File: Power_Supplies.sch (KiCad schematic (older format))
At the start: 25 parts, among them U4 BD50FC0WEFJ-E2, U5 LDL212D33R, U6 LDL212D33R

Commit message: Stuff
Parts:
- gave numbers to parts that had none: 11

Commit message: Finished schemo and placement of power supply board, then resolved interconnects with the main board.
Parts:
- removed C21: 100nF_0603_Ceramic_Capacitor,_10%,_X7R,_25V, Capacitor_SMD:C_0603_1608Metric, symbol OpenVent:100nF_0603_Ceramic_Capacitor,_10%,_X7R,_25V
- removed R11: 10k_0603_Chip_Resistor,_1%,_0.1W, Resistor_SMD:R_0603_1608Metric, symbol OpenVent:10k_0603_Chip_Resistor,_1%,_0.1W
- removed R16, R17: 1K_0603_Chip_Resistor,_1%,_0.1W, Resistor_SMD:R_0603_1608Metric, symbol OpenVent:1K_0603_Chip_Resistor,_1%,_0.1W
- removed R8: 634R_0603_Chip_Resistor,_1%,_0.1W, Resistor_SMD:R_0603_1608Metric, symbol OpenVent:634R_0603_Chip_Resistor,_1%,_0.1W
- removed R9: 20k_0603_Chip_Resistor,_1%,_0.1W, Resistor_SMD:R_0603_1608Metric, symbol OpenVent:20k_0603_Chip_Resistor,_1%,_0.1W
- added R8: R_0603_200_0.1W_1%, Resistor_SMD:R_0603_1608Metric, symbol OpenVent:R_0603_200_0.1W_1%
- added R9: R_0603_24k9_0.1W_1%, symbol OpenVent:R_0603_24k9_0.1W_1%
- U7: footprint Package_SO:VSSOP-8_3.0x3.0mm_P0.65mm -> F_ICs:Texas_S-PDSO-G8
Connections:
- net labels added: FAN_DRIVE, MICROSWITCH_1, MICROSWITCH_2, MICROSWITCH_3
- net labels removed: VIN_12V, nLINE_PWR_FAULT
- wire segments 110 -> 105
- no-connect marks 1 -> 0
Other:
- moved on the sheet: D2, U7B

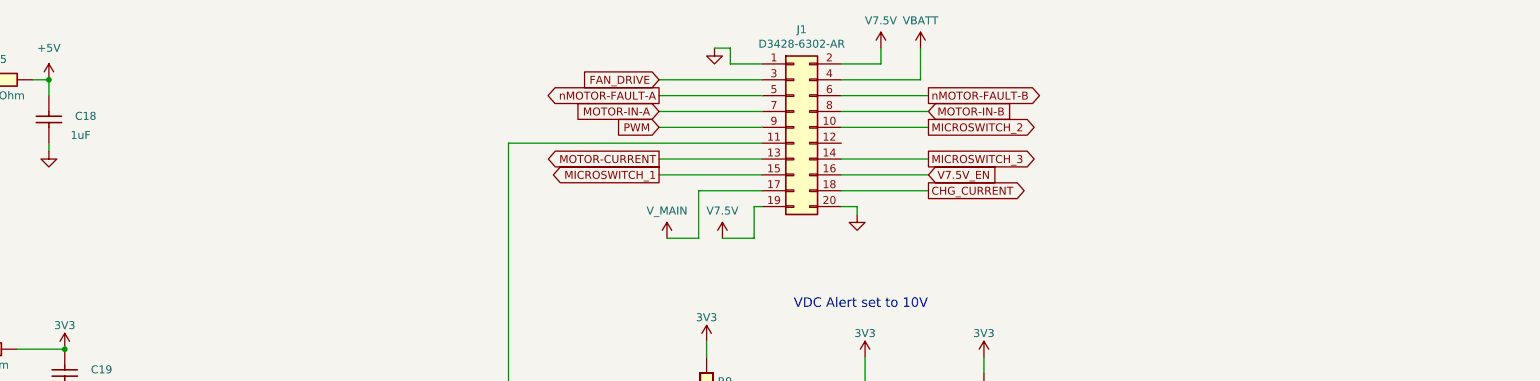
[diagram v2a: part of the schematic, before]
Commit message: Went through the whole circuit and made a note of what needs changing
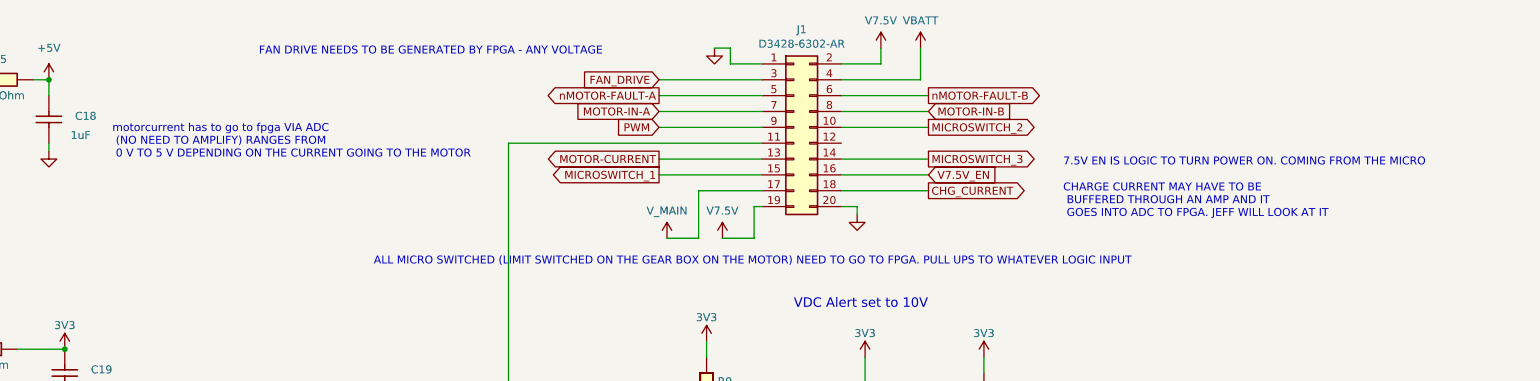
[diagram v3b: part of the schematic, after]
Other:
- note added: "7.5V EN IS LOGIC TO TURN POWER ON. COMING FROM THE MICRO"
- note added: "ALL MICRO SWITCHED (LIMIT SWITCHED ON THE GEAR BOX ON THE MOTOR) NEED TO GO TO FPGA. PULL UPS TO WHATEVER LOGIC INPUT"
- note added: "CHARGE CURRENT MAY HAVE TO BE\n BUFFERED THROUGH AN AMP AND IT\n GOES INTO ADC TO FPGA. JEFF WILL LOOK AT IT"
- note added: "FAN DRIVE NEEDS TO BE GENERATED BY FPGA - ANY VOLTAGE\n"
- note added: "motorcurrent has to go to fpga VIA ADC\n (NO NEED TO AMPLIFY) RANGES FROM\n 0 V TO 5 V DEPENDING ON THE CURRENT GOING TO THE MOTOR"
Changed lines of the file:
@@
 Wire Wire Line
 	9750 1700 9200 1700
+Text Notes 5525 1050 0    50   ~ 0
+FAN DRIVE NEEDS TO BE GENERATED BY FPGA - ANY VOLTAGE\n
+Text Notes 6250 2375 0    50   ~ 0
+ALL MICRO SWITCHED (LIMIT SWITCHED ON THE GEAR BOX ON THE MOTOR) NEED TO GO TO FPGA. PULL UPS TO WHATEVER LOGIC INPUT
+Text Notes 4600 1700 0    50   ~ 0
+motorcurrent has to go to fpga VIA ADC\n (NO NEED TO AMPLIFY) RANGES FROM\n 0 V TO 5 V DEPENDING ON THE CURRENT GOING TO THE MOTOR
+Text Notes 10600 2075 0    50   ~ 0
+CHARGE CURRENT MAY HAVE TO BE\n BUFFERED THROUGH AN AMP AND IT\n GOES INTO ADC TO FPGA. JEFF WILL LOOK AT IT
+Text Notes 10600 1750 0    50   ~ 0
+7.5V EN IS LOGIC TO TURN POWER ON. COMING FROM THE MICRO
 $EndSCHEMATC

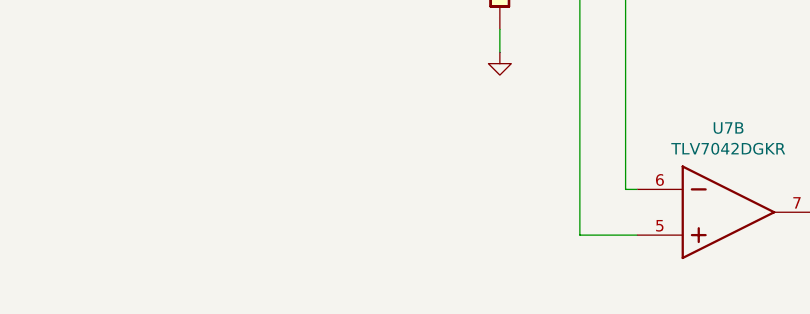
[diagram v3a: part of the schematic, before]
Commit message: Went through the Task list with Darren 1:1 with Ebony, possible new volunteer Changed gain on MPX4006DP to 8.5 gain Added a second MPXV4006GP Took sensor data off MCU: Pressure sensor (patient), oxygen sensor, flow sensor gain, flow sensor to be on FPGA only. Left alerts, battery sensor, and current measurements on MCU. Added circuit for Sensiron SM3020 and scaled output to 3v3.
Went through the Task list with Darren
1:1 with Ebony, possible new volunteer
Changed gain on MPX4006DP to 8.5 gain
Added a second MPXV4006GP
Took sensor data off MCU: Pressure sensor (patient), oxygen sensor, flow sensor gain, flow sensor to be on FPGA only. Left alerts, battery sensor, and current measurements on MCU.
Added circuit for Sensiron SM3020 and scaled output to 3v3.
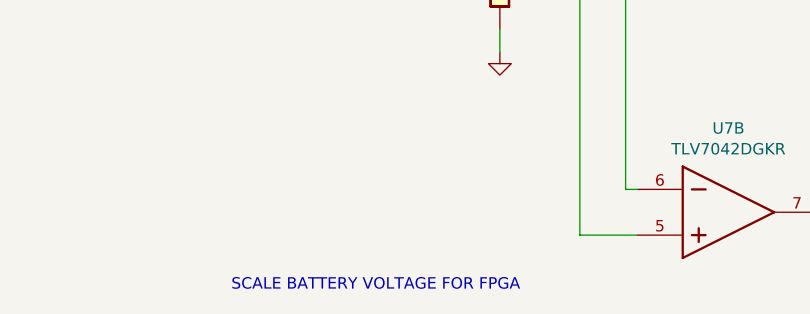
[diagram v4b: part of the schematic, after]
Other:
- note added: "SCALE BATTERY VOLTAGE FOR FPGA"
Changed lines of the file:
@@
 Text Notes 10600 1750 0    50   ~ 0
 7.5V EN IS LOGIC TO TURN POWER ON. COMING FROM THE MICRO
+Text Notes 7175 5500 0    50   ~ 0
+SCALE BATTERY VOLTAGE FOR FPGA
 $EndSCHEMATC

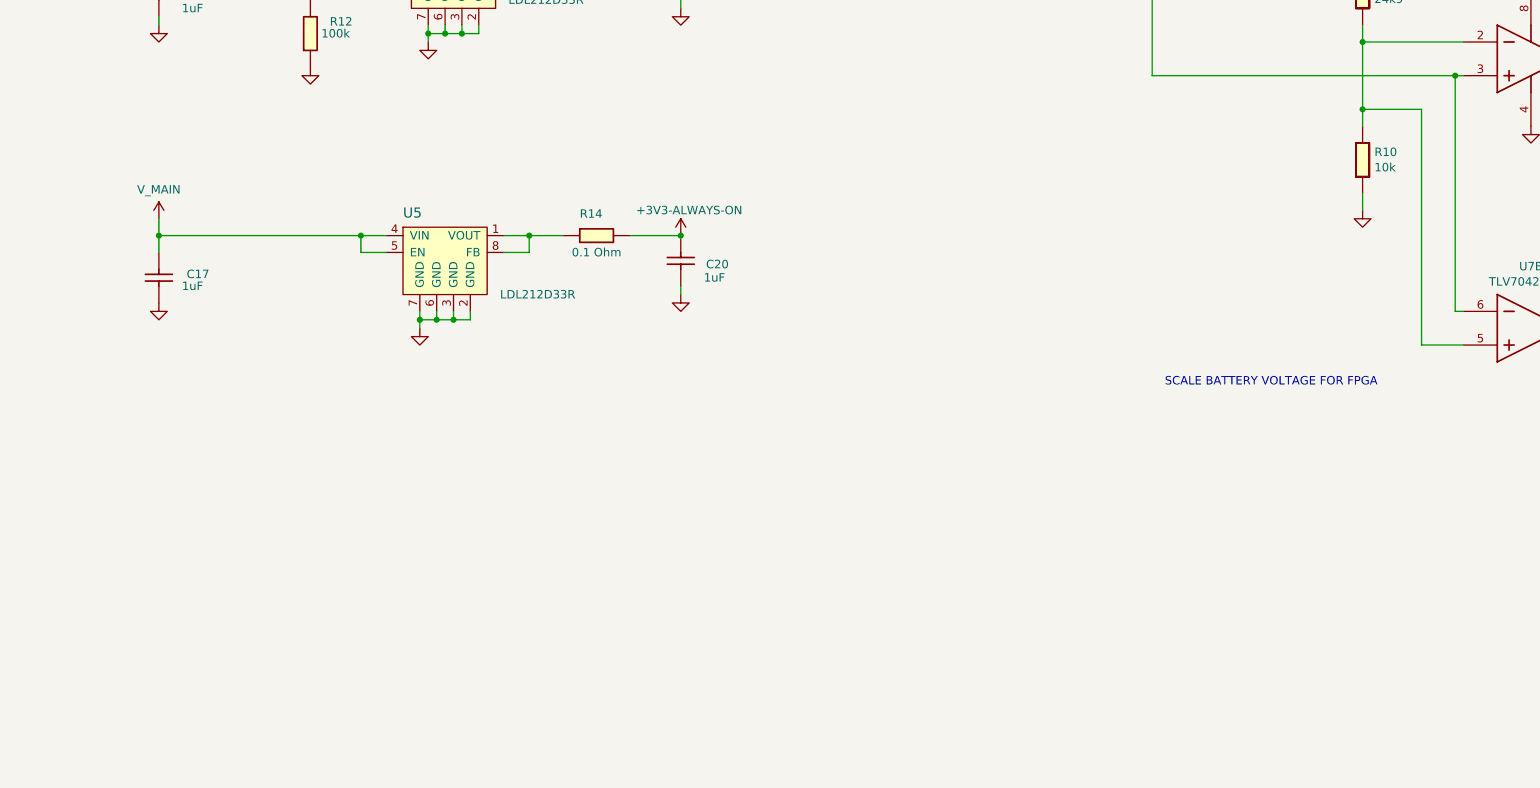
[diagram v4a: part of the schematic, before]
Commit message: Power Motor Control added. Battery voltage scale
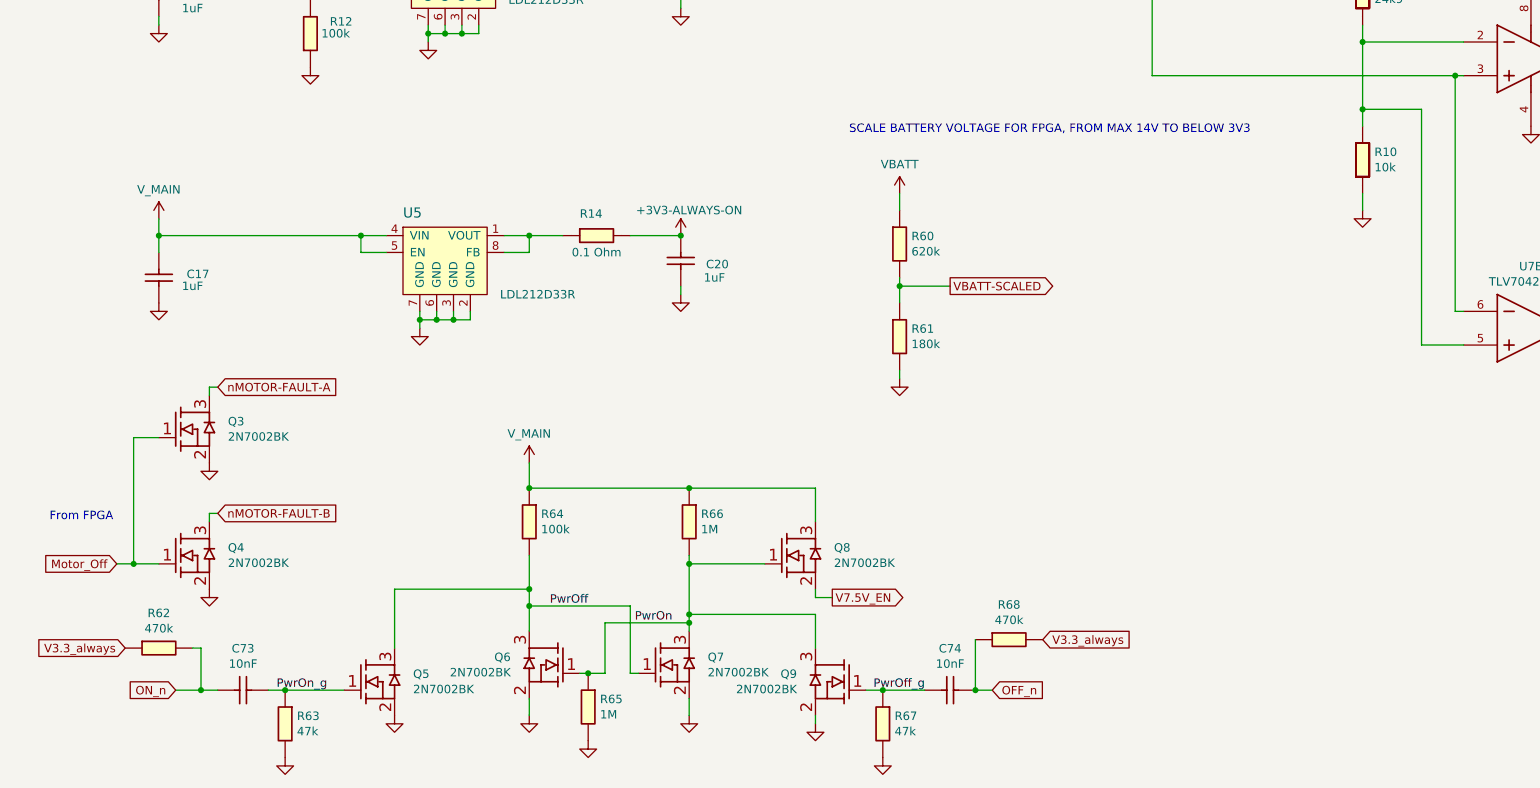
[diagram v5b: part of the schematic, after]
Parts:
- added C73, C74: 10nF_0603_Ceramic_Capacitor,_10%,_50V,_X7R-, symbol OpenVent:10nF_0603_Ceramic_Capacitor,_10%,_50V,_X7R-
- added Q3, Q4, Q5, Q6, Q7, Q8, Q9: 2N7002BK, symbol OpenVent:2N7002BK
- added R60: 620k_0603_Chip_Resistor,_1%,_0.1W, symbol OpenVent:620k_0603_Chip_Resistor,_1%,_0.1W
- added R61: 180k_0603_Chip_Resistor,_1%,_0.1W, symbol OpenVent:180k_0603_Chip_Resistor,_1%,_0.1W
- added R62, R68: 470k_0603_Chip_Resistor,_1%,_0.1W, symbol OpenVent:470k_0603_Chip_Resistor,_1%,_0.1W
- added R63, R67: 47k_0603_Chip_Resistor,_1%,_0.1W, symbol OpenVent:47k_0603_Chip_Resistor,_1%,_0.1W
- added R64: 100K_0603_Chip_Resistor,_1%,_0.1W, symbol OpenVent:100K_0603_Chip_Resistor,_1%,_0.1W
- added R65, R66: 1M_0603_Chip_Resistor,_1%,_0.1W, symbol OpenVent:1M_0603_Chip_Resistor,_1%,_0.1W
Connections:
- net GND: now also Q3.2 (S), Q4.2 (S), Q5.2 (S), Q6.2 (S), Q7.2 (S), Q9.2 (S), R61.2, R63.2, R65.2, R67.2
- net V7.5V_EN: now also Q8.2 (S)
- net nMOTOR-FAULT-A: now also Q3.3 (D)
- net nMOTOR-FAULT-B: now also Q4.3 (D)
- new net Motor_Off: Q3.1 (G1), Q4.1 (G1)
- new net OFF_n: C74.2, R68.1
- new net ON_n: C73.1, R62.2
- new net PwrOff: Q5.3 (D), Q6.3 (D), Q7.1 (G1), R64.2
- new net PwrOff_g: C74.1, Q9.1 (G1), R67.1
- new net PwrOn: Q6.1 (G1), Q7.3 (D), Q8.1 (G1), Q9.3 (D), R65.1, R66.2
- new net PwrOn_g: C73.2, Q5.1 (G1), R63.1
- new net V3.3_always: R62.1, R68.2
- new net VBATT: R60.1
- new net VBATT-SCALED: R60.2, R61.1
- new net V_MAIN: Q8.3 (D), R64.1, R66.1
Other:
- note added: "From FPGA"
- note added: "SCALE BATTERY VOLTAGE FOR FPGA, FROM MAX 14V TO BELOW 3V3"
- note removed: "SCALE BATTERY VOLTAGE FOR FPGA"
